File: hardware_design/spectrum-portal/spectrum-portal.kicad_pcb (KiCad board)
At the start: 2 copper layers, 32.1 x 117.2 mm, 28 parts, among them J1 PJ398SM, J2 PJ398SM, J3 Conn_Coaxial, J4 PJ398SM, J5 PJ398SM, J6 Conn_Coaxial, J7 SBH11-PBPC-D05-ST-BK, U1 TL072

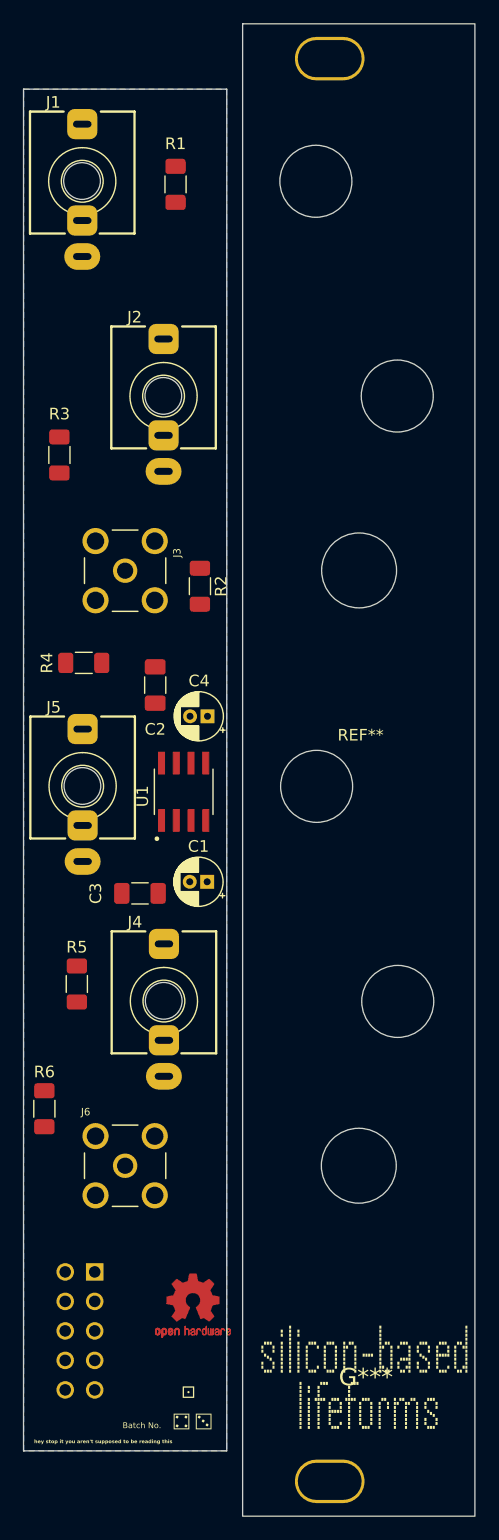
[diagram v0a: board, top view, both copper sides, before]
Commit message: Redesigned as 5HP, added protection components
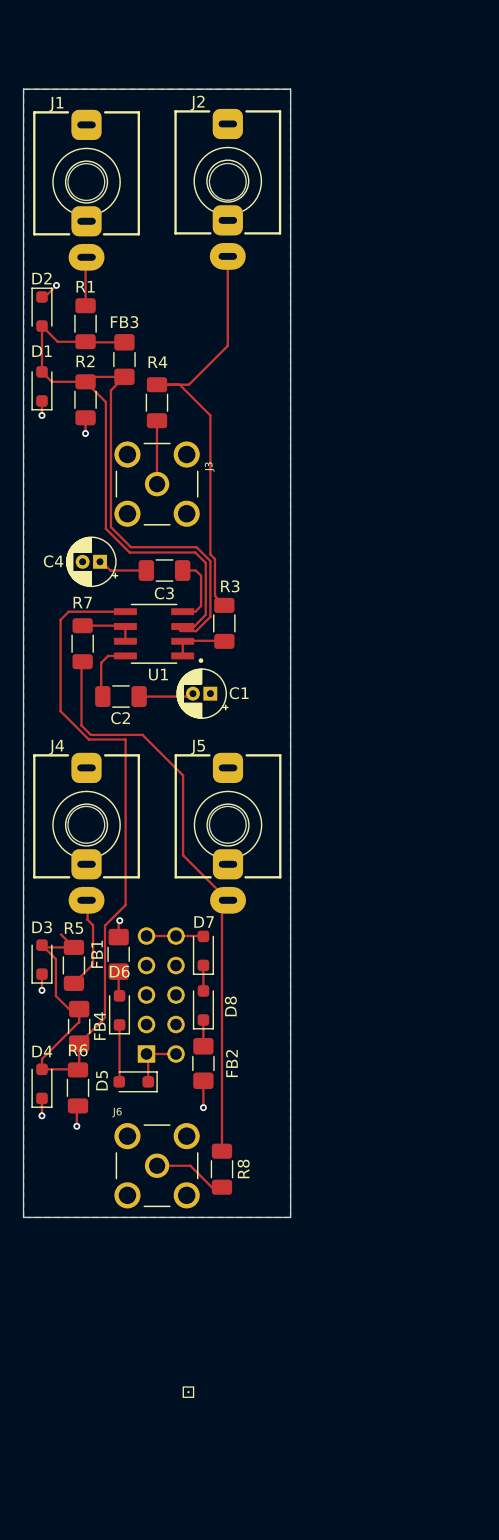
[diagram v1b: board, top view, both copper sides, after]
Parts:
- removed G*** (x3): LOGO, LOGO
- removed REF** (x4): Faceplate_Hole_3.5mm_Jack, Eurorack:Faceplate_Hole_3.5mm_Jack
- removed REF**: Faceplate_4HP_Mounting_Slots, Eurorack:Faceplate_4HP_Mounting_Slots
- removed REF** (x2): OSHW-Logo2_7.3x6mm_Copper, Symbol:OSHW-Logo2_7.3x6mm_Copper
- added D1: PJGBLC15C_R1_00001, Diode_SMD:D_SOD-323_HandSoldering, F.Cu at (108.0, 83.6)
- added D2: PJGBLC15C_R1_00001, Diode_SMD:D_SOD-323_HandSoldering, F.Cu at (108.0, 77.2)
- added D3: PJGBLC15C_R1_00001, Diode_SMD:D_SOD-323_HandSoldering, F.Cu at (108.0, 133.0)
- added D4: PJGBLC15C_R1_00001, Diode_SMD:D_SOD-323_HandSoldering, F.Cu at (108.0, 143.7)
- added D5: NSR0530HT1G, Diode_SMD:D_SOD-323_HandSoldering, F.Cu at (115.9, 143.5)
- added D6: D12V0H1U2WS-7, Diode_SMD:D_SOD-323_HandSoldering, F.Cu at (114.7, 137.3)
- added D7: NSR0530HT1G, Diode_SMD:D_SOD-323_HandSoldering, F.Cu at (121.9, 132.2)
- added D8: D12V0H1U2WS-7, Diode_SMD:D_SOD-323_HandSoldering, F.Cu at (121.9, 136.9)
- added FB1: 2512066017Y1, Inductor_SMD:L_1206_3216Metric_Pad1.42x1.75mm_HandSolder, F.Cu at (114.6, 132.5)
- added FB2: 2512066017Y1, Inductor_SMD:L_1206_3216Metric_Pad1.42x1.75mm_HandSolder, F.Cu at (121.9, 141.9)
- added FB3: 2512066017Y1, Inductor_SMD:L_1206_3216Metric_Pad1.42x1.75mm_HandSolder, F.Cu at (115.1, 81.3)
- added FB4: 2512066017Y1, Inductor_SMD:L_1206_3216Metric_Pad1.42x1.75mm_HandSolder, F.Cu at (111.2, 138.7)
- added R1: 1KΩ, Resistor_SMD:R_1206_3216Metric_Pad1.30x1.75mm_HandSolder, F.Cu at (111.8, 78.2)
- added R5: 1KΩ, Resistor_SMD:R_1206_3216Metric_Pad1.30x1.75mm_HandSolder, F.Cu at (110.8, 133.4)
- J3, J6: value Conn_Coaxial -> J998-ND
- R2: renamed from R1; value 10MΩ -> 100KΩ
- R6: renamed from R4; value 10MΩ -> 100KΩ
- U1: value TL072 -> TL072IDR
- moved R6 36.6 mm to (111.1, 144.0), turned to -90 degrees
- moved J7 29.8 mm to (118.3, 136.0), turned to 90 degrees
- moved R7 29.3 mm to (111.5, 105.8)
- moved C3 27.9 mm to (118.5, 99.5), turned to 180 degrees
- moved R2 20.1 mm to (111.8, 84.8), turned to -90 degrees
- moved J2 19.3 mm to (124.0, 65.9)
- moved J4 16.6 mm to (111.8, 121.4)
- moved C1 16.2 mm to (122.5, 110.0)
- moved C4 16.2 mm to (113.0, 98.7)
- moved R8 16.2 mm to (123.5, 151.0)
- moved U1 13.8 mm to (117.7, 104.9), turned to 180 degrees
- moved J5 13.0 mm to (124.0, 121.4)
- moved R4 9.53 mm to (117.9, 85.0)
- moved J3 7.94 mm to (117.9, 92.0)
- moved R3 3.83 mm to (123.7, 104.0), turned to 90 degrees
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- renumbered R2 to R3, R3 to R4, R5 to R7, R6 to R8
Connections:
- J1 pad S: Net-(U1B--) -> Net-(J1-PadS)
- J2 pad S: Net-(U1B-+) -> Net-(J2-PadS)
- J4 pad S: Net-(U1B-+) -> Net-(J4-PadS)
- J5 pad S: Net-(U1B--) -> Net-(J5-PadS)
- J7 pad 1: -12V -> Net-(D5-K)
- J7 pad 10: +12V -> Net-(D7-A)
- J7 pad 2: -12V -> Net-(D5-K)
- J7 pad 9: +12V -> Net-(D7-A)
- R3 pad 1: Net-(R2-Pad1) -> Net-(U1A--)
- R3 pad 2: Net-(U1A--) -> Net-(J2-PadS)
- R4 pad 2: Net-(U1A--) -> Net-(J2-PadS)
- R7 pad 1: Net-(R5-Pad1) -> Net-(U1B--)
- R7 pad 2: Net-(U1B--) -> Net-(J5-PadS)
- R8 pad 2: Net-(U1B--) -> Net-(J5-PadS)
- U1 pad 1: Net-(R2-Pad1) -> Net-(U1A--)
- U1 pad 7: Net-(R5-Pad1) -> Net-(U1B--)
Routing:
- net Net-(J5-PadS): track 0.00 -> 51.0 mm
- net Net-(U1B-+): track 0.00 -> 50.4 mm
- net Net-(D1-A): track 0.00 -> 45.9 mm
- net Net-(J2-PadS): track 0.00 -> 36.9 mm
- net Net-(U1A-+): track 0.00 -> 34.3 mm
- net Net-(D3-A): track 0.00 -> 21.4 mm
- net Net-(J4-PadS): track 0.00 -> 8.07 mm
- net Net-(J6-In): track 0.00 -> 6.36 mm
- net Net-(U1C-V-): track 0.00 -> 6.16 mm
- net Net-(J3-In): track 0.00 -> 5.46 mm
- net Net-(U1C-V+): track 0.00 -> 5.31 mm
- net Net-(D5-K): track 0.00 -> 5.00 mm
- net Net-(D7-A): track 0.00 -> 4.91 mm
- net Net-(D5-A): track 0.00 -> 4.91 mm
- net Net-(C1-Pad2): track 0.00 -> 4.74 mm
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- added copper zone on In2.Cu, net +12V
- added copper zone on B.Cu, net -12V
- added copper zone on In1.Cu, net GND
- removed copper zone on B.Cu, net GND
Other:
- board size 32.1 x 117.2 mm -> 23 x 97.2 mm
- copper layers 2 -> 4
- board text removed: "+12V"
- board text removed: "Batch No."
- board text removed: "Faceplate"
- board text removed: "hey stop it you aren't supposed to be reading this"

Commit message: Switch to more affordable SMA connector
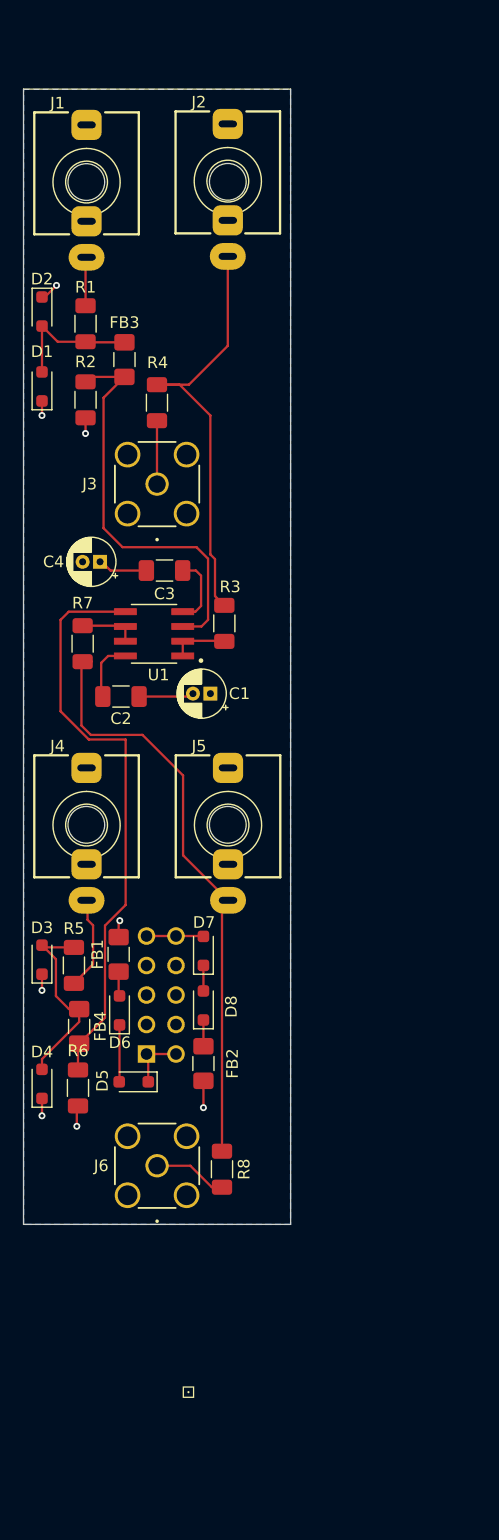
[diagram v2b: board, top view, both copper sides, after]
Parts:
- J3, J6: value J998-ND -> ~; footprint SMA:LINX_CONSMA008-G -> SMA:CONN_132291_AMP
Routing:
- net Net-(D1-A): track 45.9 -> 11.7 mm
- net Net-(D3-A): track 21.4 -> 16.7 mm
- net Net-(U1B-+): track 50.4 -> 50.9 mm
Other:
- board size 23 x 97.2 mm -> 23 x 97.8 mm
